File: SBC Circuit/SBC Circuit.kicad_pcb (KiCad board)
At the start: 2 copper layers, 139.7 x 114.3 mm, 81 parts, among them J1 USB_B, J2 Conn_01x02_Pin, J3 Conn_01x06_Pin, J4 Conn_01x06_Pin, J5 Conn_01x03_Pin, J6 Conn_01x08_Pin, J7 Conn_01x06_Pin, J8 Conn_01x02_Pin, J9 Conn_02x04_Odd_Even, Q1 AOI21357, Q2 AOI21357, SW1 RESET, U1 MC68000FN, U10 FT230XS, U11 MC34064P, U2 XC9572XL, U3 68681, U4 MCM6206CP, U5 MCM6206CP, U6 28C256, U7 28C256, U8 LM7805_TO220, U9 LD1117AV33, X1 SG-531, X2 EC11

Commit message: Begin wiring DUART
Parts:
- moved C25 112.1 mm to (-534.5, 77.0), turned to -90 degrees
- moved C24 106.4 mm to (-534.5, 73.5)
- moved U7 103.8 mm to (-530.6, 90.1)
- moved C23 102.9 mm to (-576.9, 73.5)
- moved C22 101.5 mm to (-576.9, 77.0), turned to -90 degrees
- moved U6 96.4 mm to (-573.0, 90.1)
- moved U5 81.7 mm to (-461.0, 196.8)
- moved U4 81.7 mm to (-461.0, 215.7)
- moved C18 81.7 mm to (-463.2, 204.7)
- moved C19 81.7 mm to (-458.7, 204.7)
- moved C20 81.7 mm to (-463.4, 185.8)
- moved C21 81.7 mm to (-458.9, 185.8)
- moved C8 17.0 mm to (-401.3, 86.9)
- moved C10 17.0 mm to (-425.4, 109.3)
- moved C11 17.0 mm to (-425.4, 113.8)
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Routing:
- net addr0: track 0.00 -> 75.4 mm
- net addr2: track 0.00 -> 75.0 mm
- net addr1: track 0.00 -> 74.6 mm
- net addr3: track 0.00 -> 73.7 mm
- net +5V: track 217.3 -> 253.3 mm
- net +3.3V: track 138.9 -> 171.8 mm
- net duart_iack: track 0.00 -> 26.8 mm
- net duart_cs: track 0.00 -> 22.5 mm
- net hlt_rst: track 27.2 -> 43.6 mm
- net data7: track 0.00 -> 10.4 mm
- net data5: track 0.00 -> 10.4 mm
- net data3: track 0.00 -> 10.4 mm
- net data1: track 0.00 -> 10.4 mm
- net /Memory+Peripheral/rw: track 0.00 -> 8.20 mm
- net data4: track 0.00 -> 7.37 mm
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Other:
- board size 139.7 x 114.3 mm -> 127 x 114.3 mm
- board text added: "5.0x4.5{dblquote}"
- board text added: "Made in xxx"
- board text added: "designed by Richard Homan mm/dd/2024 — revision 0.0"
- board text removed: "4.5x5.5{dblquote}"

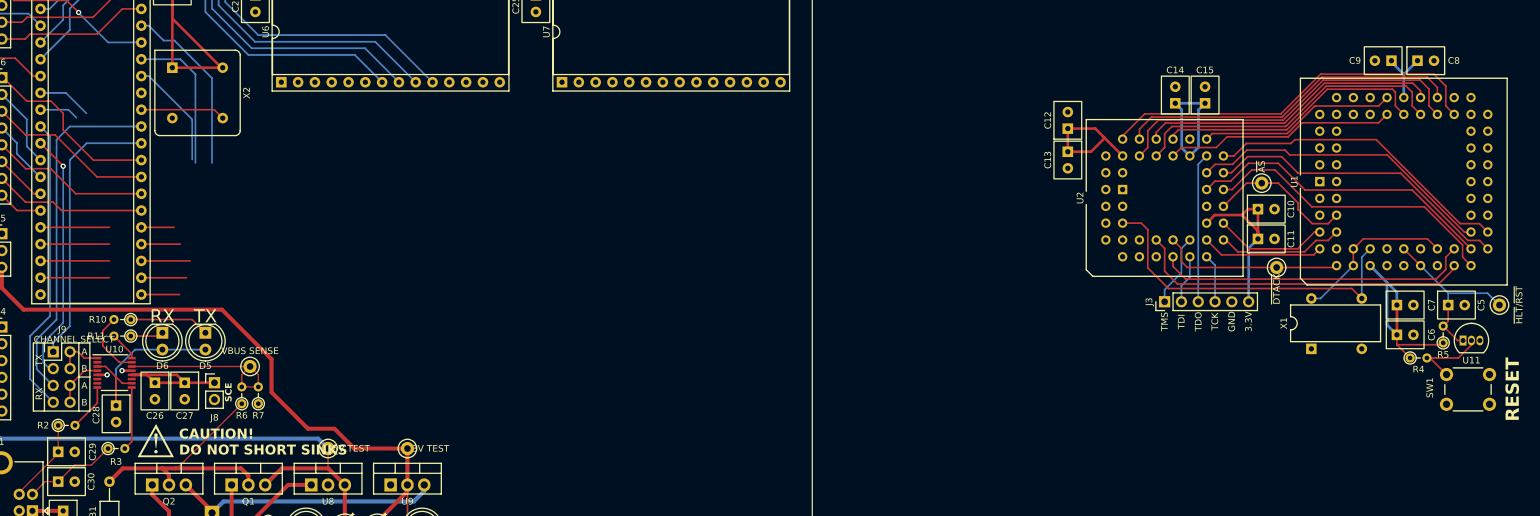
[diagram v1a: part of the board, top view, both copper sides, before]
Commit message: Complete DUART lines
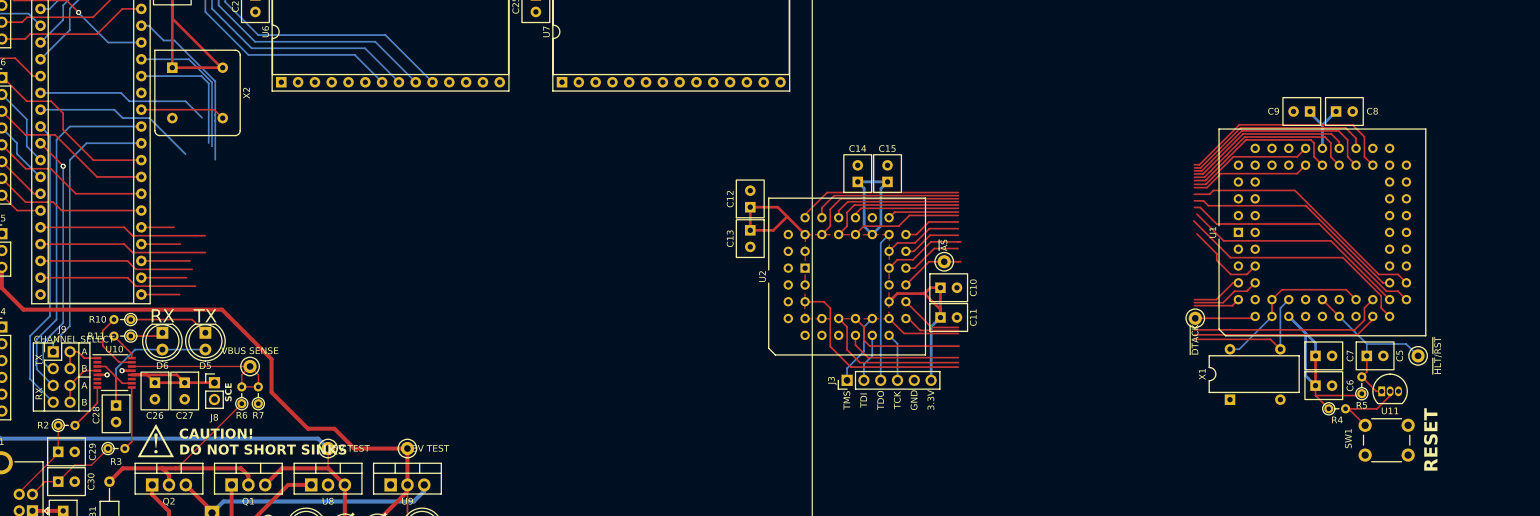
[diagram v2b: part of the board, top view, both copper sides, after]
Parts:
- moved C10 49.4 mm to (-473.4, 121.2)
- moved C11 49.4 mm to (-473.4, 125.7)
- moved C12 49.4 mm to (-502.1, 109.0)
- moved C13 49.4 mm to (-502.1, 112.5)
- moved C14 49.4 mm to (-485.9, 105.2)
- moved C15 49.4 mm to (-481.4, 105.2)
- moved J3 49.4 mm to (-487.5, 135.2)
- moved TP5 49.4 mm to (-472.8, 117.3)
- moved U2 49.4 mm to (-493.9, 118.2)
- moved C5 14.5 mm to (-408.9, 131.5)
- moved C6 14.5 mm to (-416.7, 136.0)
- moved C7 14.5 mm to (-416.7, 131.5)
- moved C9 14.5 mm to (-417.5, 94.6)
- moved R4 14.5 mm to (-414.7, 139.5)
- moved R5 14.5 mm to (-409.7, 137.2)
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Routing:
- net duart_dtack: track 5.93 -> 24.7 mm
- net /Memory+Peripheral/rw: track 8.20 -> 26.0 mm
- net data3: track 10.4 -> 25.4 mm
- net data1: track 10.4 -> 25.4 mm
- net data7: track 10.4 -> 23.9 mm
- net data5: track 10.4 -> 23.4 mm
- net hlt_rst: track 43.6 -> 46.8 mm
- net duart_cs: track 22.5 -> 21.8 mm
- added copper zone on F.Cu, net +3.3V

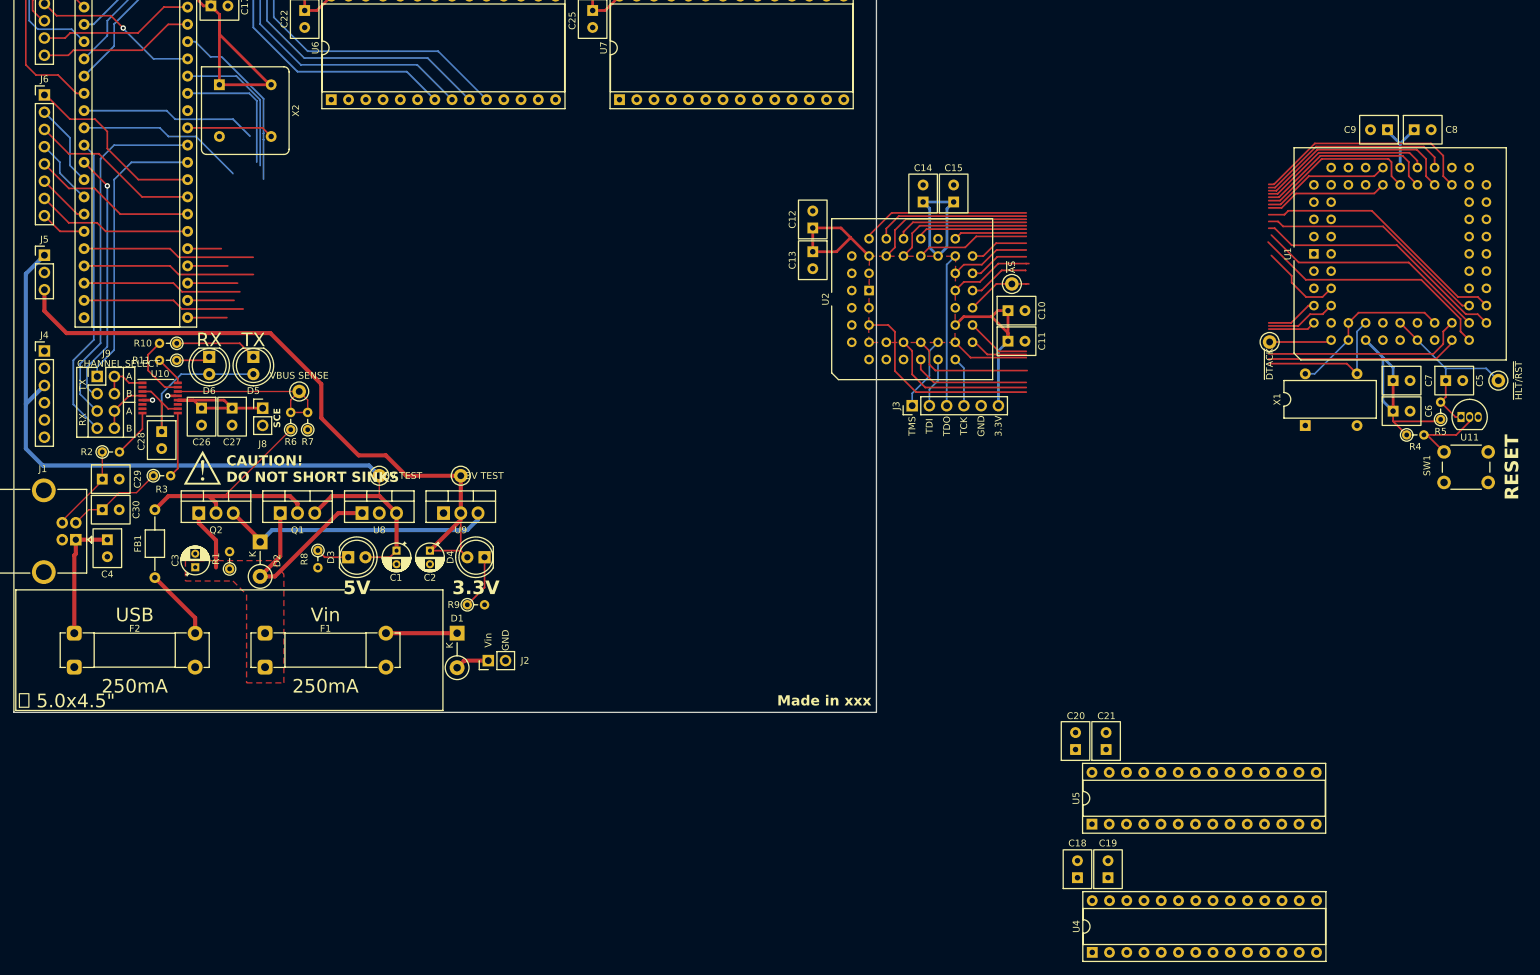
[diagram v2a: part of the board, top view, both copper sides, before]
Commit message: Finish DUART lines
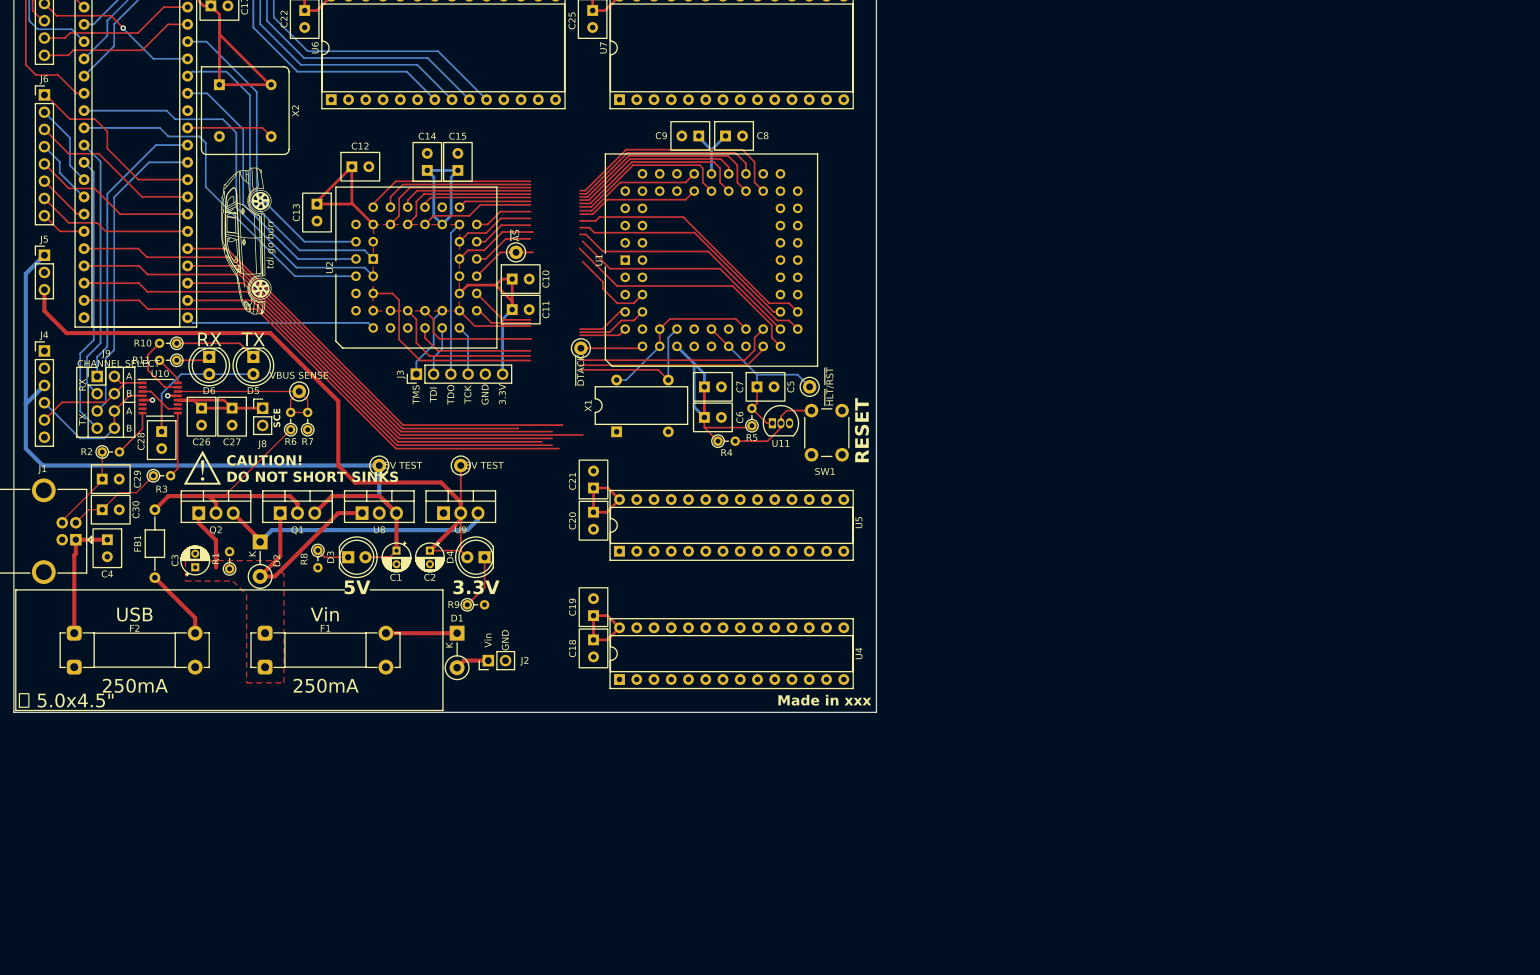
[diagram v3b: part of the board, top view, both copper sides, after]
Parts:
- added G***: LOGO, LOGO, F.Cu at (-586.0, 111.0)
- moved C6 101.4 mm to (-518.1, 136.9)
- moved C7 101.4 mm to (-518.1, 132.4)
- moved C9 101.4 mm to (-518.9, 95.5)
- moved R4 101.4 mm to (-516.1, 140.4)
- moved C5 101.4 mm to (-510.3, 132.4)
- moved C8 101.4 mm to (-515.0, 95.5)
- moved R5 101.4 mm to (-511.1, 138.1)
- moved TP3 101.4 mm to (-502.6, 132.4)
- moved TP6 101.4 mm to (-536.3, 126.7)
- moved U1 101.4 mm to (-529.8, 113.8)
- moved U11 101.4 mm to (-508.1, 137.8)
- moved X1 101.4 mm to (-531.0, 139.0)
- moved SW1 93.1 mm to (-502.3, 142.4), turned to 90 degrees
- moved C19 85.0 mm to (-534.4, 166.1)
- moved C21 84.7 mm to (-534.4, 147.3)
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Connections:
- J9 pad 1: tx_a -> rx_a
- J9 pad 2: /Power+IO/rx_s -> /Power+IO/tx_s
- J9 pad 3: tx_b -> rx_b
- J9 pad 4: /Power+IO/rx_s -> /Power+IO/tx_s
- J9 pad 5: rx_a -> tx_a
- J9 pad 6: /Power+IO/tx_s -> /Power+IO/rx_s
- J9 pad 7: rx_b -> tx_b
- J9 pad 8: /Power+IO/tx_s -> /Power+IO/rx_s
- U2 pad 1: duart_irq -> duart_cs
- U2 pad 11: unconnected-(U2-P11-Pad11) -> ramh_cs
- U2 pad 2: duart_iack -> duart_dtack
- U2 pad 3: duart_cs -> duart_rw
- U2 pad 4: duart_dtack -> we
- U2 pad 40: unconnected-(U2-P40/GTS2-Pad40) -> roml_cs
- U2 pad 42: hlt_rst -> duart_iack
- U2 pad 43: oe -> romh_cs
- U2 pad 44: we -> hlt_rst
- U2 pad 6: romh_cs -> oe
- U2 pad 7: roml_cs -> duart_irq
- U2 pad 8: ramh_cs -> unconnected-(U2-P8-Pad8)
- U3 pad 8: /Memory+Peripheral/rw -> duart_rw
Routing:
- net data0: track 4.95 -> 66.0 mm
- net duart_rw: track 0.00 -> 59.1 mm
- net data3: track 25.4 -> 83.7 mm
- net data2: track 5.91 -> 63.8 mm
- net data4: track 7.37 -> 63.2 mm
- net data6: track 6.83 -> 62.5 mm
- net data7: track 23.9 -> 79.0 mm
- net data5: track 23.4 -> 77.1 mm
- net data1: track 25.4 -> 74.9 mm
- net +5V: track 253.3 -> 283.2 mm
- net duart_dtack: track 24.7 -> 53.1 mm
- net duart_cs: track 21.8 -> 48.1 mm
- net /Memory+Peripheral/rw: track 26.0 -> 0.00 mm
- net duart_irq: track 5.79 -> 28.0 mm
- net hlt_rst: track 46.8 -> 68.5 mm
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
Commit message: Update revision notes and time sheet
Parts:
- moved C18 696.7 mm to (161.5, 137.0)
- moved C19 696.7 mm to (161.5, 133.4)
- moved C20 696.7 mm to (161.5, 118.2)
- moved C21 696.7 mm to (161.5, 114.6)
- moved C22 696.7 mm to (119.0, 44.3)
- moved C23 696.7 mm to (119.0, 40.8)
- moved C6 696.7 mm to (177.8, 104.3)
- moved C7 696.7 mm to (177.8, 99.8)
- moved C9 696.7 mm to (177.0, 62.8)
- moved D4 696.7 mm to (145.5, 124.8)
- moved J1 696.7 mm to (85.3, 122.3)
- moved R3 696.7 mm to (96.7, 112.8)
- moved R4 696.7 mm to (179.8, 107.8)
- moved TP1 696.7 mm to (130.0, 111.3)
- moved TP2 696.7 mm to (142.0, 111.3)
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
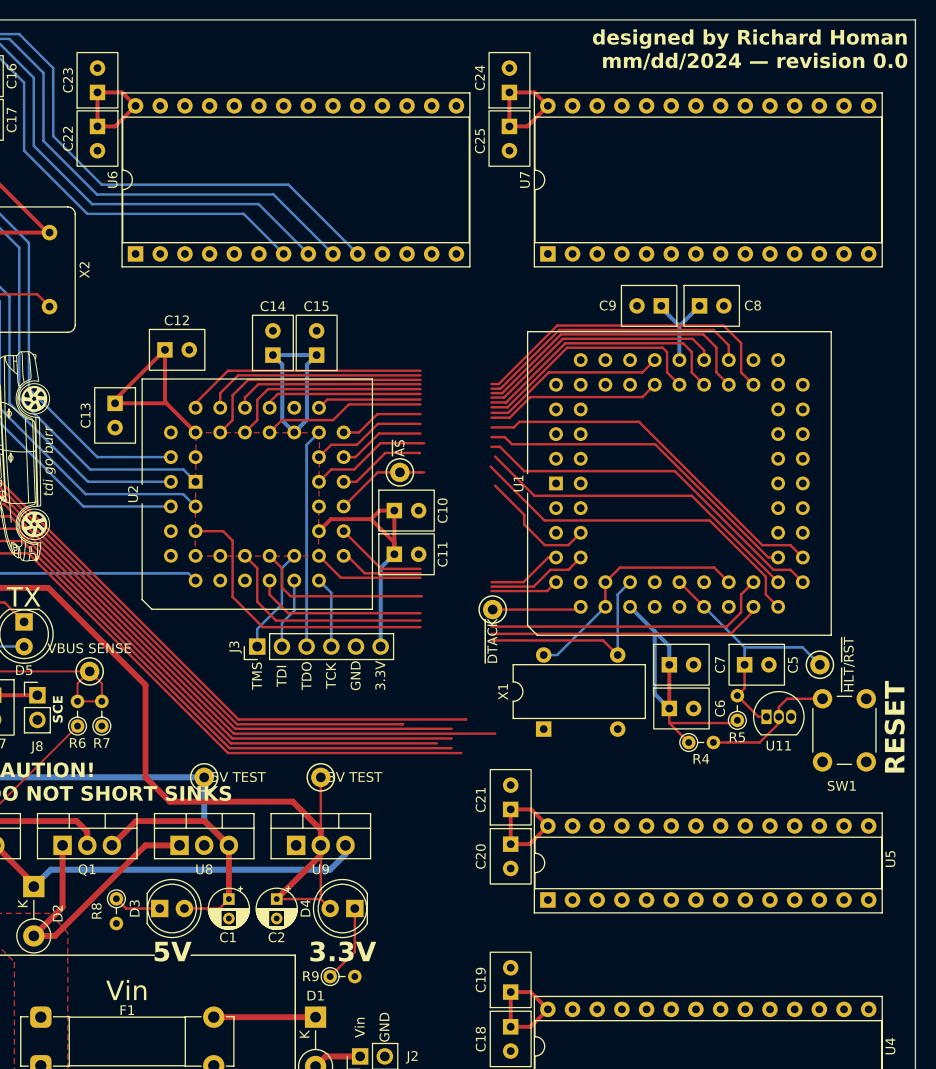
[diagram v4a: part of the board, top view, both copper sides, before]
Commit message: ROM high connected
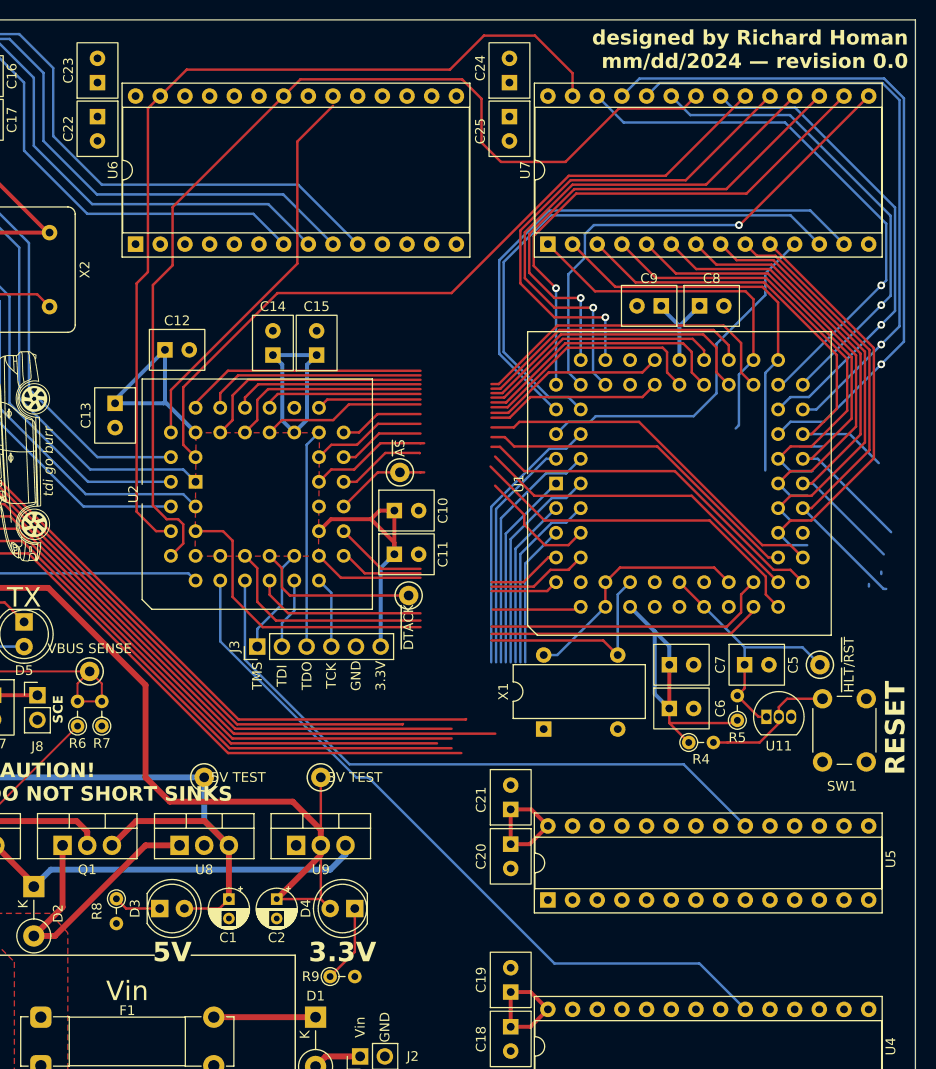
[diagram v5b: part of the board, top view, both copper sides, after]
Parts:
- moved TP6 8.77 mm to (151.0, 92.6)
- moved C22 1.01 mm to (119.0, 43.3)
- moved C23 1.01 mm to (119.0, 39.8)
- moved C24 1.01 mm to (161.4, 39.8)
- moved C25 1.01 mm to (161.4, 43.3)
- moved U6 1.01 mm to (122.9, 56.5)
- moved U7 1.01 mm to (165.3, 56.5)
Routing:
- net oe: track 0.00 -> 107.5 mm
- net we: track 0.00 -> 97.1 mm
- net romh_cs: track 0.00 -> 78.0 mm
- net raml_cs: track 0.00 -> 76.0 mm
- net addr8: track 0.00 -> 74.9 mm, vias 0 -> 1
- net ramh_cs: track 0.00 -> 66.7 mm
- net addr9: track 0.00 -> 64.1 mm, vias 0 -> 1
- net data10: track 0.00 -> 56.9 mm
- net addr13: track 0.00 -> 56.6 mm, vias 0 -> 1
- net data9: track 0.00 -> 55.3 mm
- net data14: track 0.00 -> 55.1 mm, vias 0 -> 1
- net data12: track 0.00 -> 54.2 mm, vias 0 -> 1
- net data13: track 0.00 -> 52.5 mm, vias 0 -> 1
- net data11: track 0.00 -> 51.9 mm, vias 0 -> 1
- net data15: track 0.00 -> 51.5 mm, vias 0 -> 1
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
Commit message: Commit before design change
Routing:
- net /ipl0: track 46.7 -> 54.6 mm
- net /fc0: track 46.5 -> 54.4 mm
- net /ipl1: track 45.7 -> 53.6 mm
- net /fc2: track 47.0 -> 54.8 mm
- net /fc1: track 46.8 -> 54.2 mm
- net /as: track 22.2 -> 29.5 mm
- net addr20: track 41.1 -> 47.9 mm
- net addr15: track 58.8 -> 65.5 mm
- net addr22: track 34.9 -> 41.7 mm
- net addr21: track 29.9 -> 36.6 mm
- net addr19: track 48.5 -> 55.3 mm
- net addr17: track 54.9 -> 61.7 mm
- net addr18: track 45.6 -> 52.3 mm
- net addr16: track 52.0 -> 58.7 mm
- net data7: track 107.3 -> 110.1 mm
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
